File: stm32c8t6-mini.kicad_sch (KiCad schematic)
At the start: 40 parts, among them J1 Conn_01x07_Pin, J2 Conn_01x18_Pin, J3 Conn_01x18_Pin, P1 USB, SW1 Reset, SW2 BOOT0, U1 STM32F103C8Tx, U2 AMS1117, U3 USBLC6-2SC6, Y1 8MHz, Y2 32.768kHz

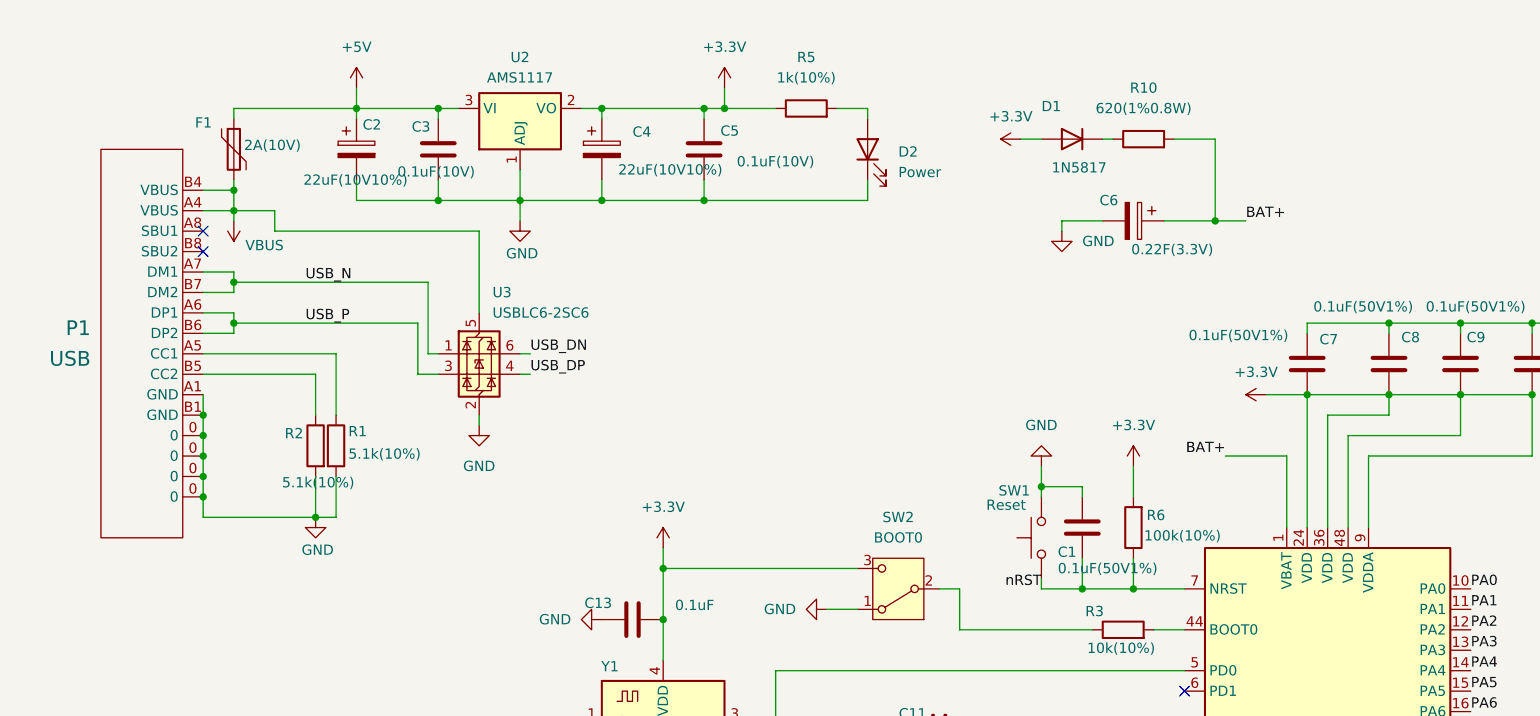
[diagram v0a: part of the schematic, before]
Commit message: Replace the USB-C socket type
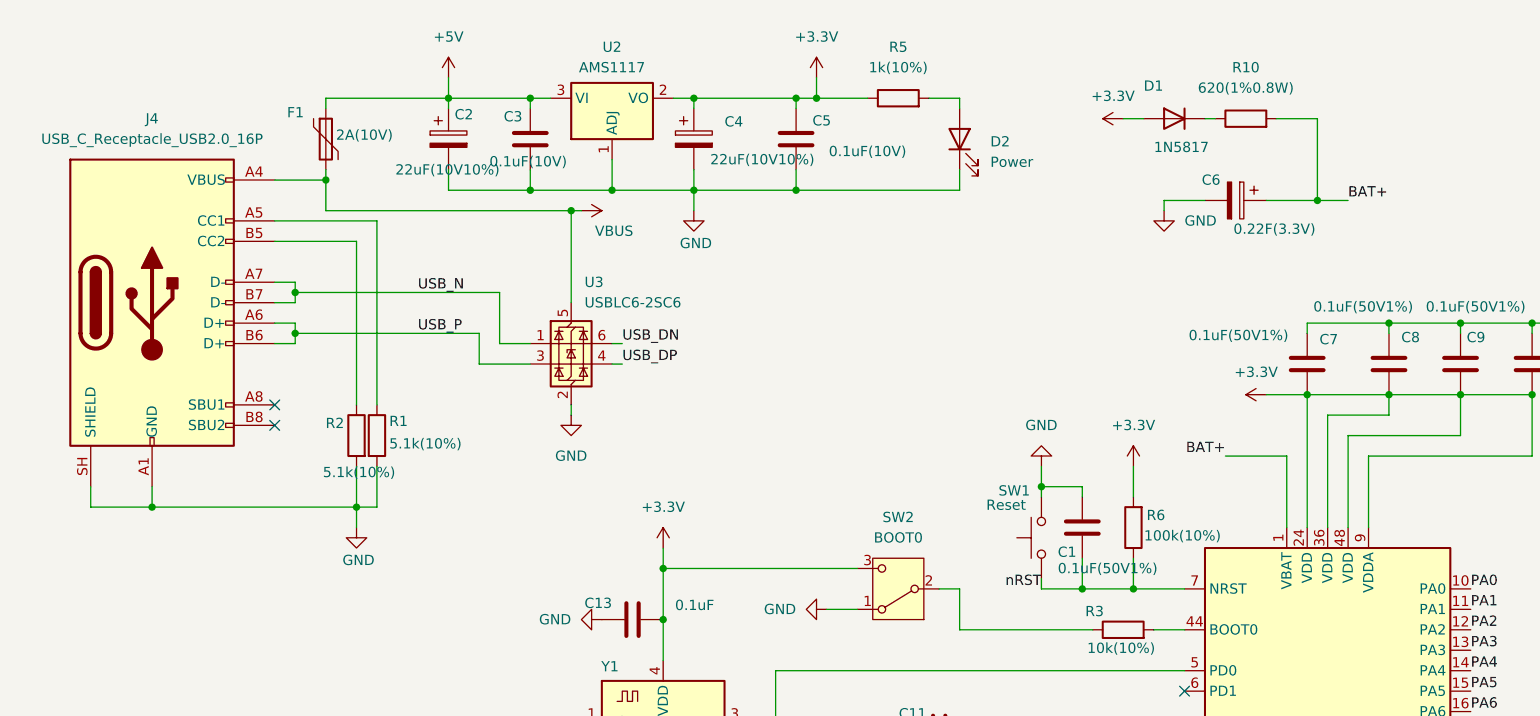
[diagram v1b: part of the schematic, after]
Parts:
- removed P1: USB, WCH:TYPE-C-Receptacle-2.0, symbol WCH:USBC-REC
- added J4: USB_C_Receptacle_USB2.0_16P, Connector_USB:USB_C_Receptacle_HRO_TYPE-C-31-M-12, symbol Connector:USB_C_Receptacle_USB2.0_16P
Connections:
- net GND: now also J4.A1 (GND), J4.A12 (GND), J4.B1 (GND), J4.B12 (GND), J4.SH (SHIELD)
- net USB_N: now also J4.A7 (D-), J4.B7 (D-)
- net USB_P: now also J4.A6 (D+), J4.B6 (D+)
- net VBUS: now also J4.A4 (VBUS), J4.A9 (VBUS), J4.B4 (VBUS), J4.B9 (VBUS)
- net at R1.1: now also J4.A5 (CC1)
- net at R2.1: now also J4.B5 (CC2)
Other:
- moved on the sheet: C2, C3, C4, C5, C6, D1, D2, F1, R1, R10, R2, R5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

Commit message: Add description to the sheet
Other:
- company: (none) -> Yongci
- title: (none) -> STM32C8T6-Mini
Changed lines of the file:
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@@
 	(generator_version "10.0")
 	(paper "A4")
+	(title_block
+		(title "STM32C8T6-Mini")
+		(date "2026-09-13")
+		(rev "v1.2")
+		(company "Yongci")
+		(comment 1 "zhuyongci@github.com")
+	)
 	(junction
 		(at 45.72 52.07)

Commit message: Replace some components: 1. Replace the RTC super-capacitance to a 5.5mAh battery. 2. Replace the 1N5817-diode to 1SS367. 3. Replace the resister size from 0805 to 0603(0.1w~).
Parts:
- removed C6: 0.22F(3.3V), Battery:BatteryHolder_Seiko_MS621F, symbol Device:C_Polarized
- added BT1: MS621FE,5.5mAh,3.3V, Battery:BatteryHolder_Seiko_MS621F, symbol Device:Battery_Cell
- D1: value 1N5817 -> 1SS367; footprint Diode_SMD:D_SOD-123 -> Diode_SMD:D_SOD-323
- R10: value 620(1%0.8W) -> 620R(1%0.1W); footprint Resistor_SMD:R_0805_2012Metric -> Resistor_SMD:R_0603_1608Metric
- renumbered C11 to C10, C12 to C11, C13 to C12, C7 to C6, C8 to C7, C9 to C8, C10 to C9
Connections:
- net BAT+: now also BT1.1 (+)
- net GND: now also BT1.2 (-)
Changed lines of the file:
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@@
 	(title_block
 		(title "STM32C8T6-Mini")
-		(date "2026-09-13")
-		(rev "v1.2")
+		(date "2026-09-20")
+		(rev "v1.3")
 		(company "Yongci")
 		(comment 1 "zhuyongci@hotmail.com")
@@
 		(in_pos_files yes)
 		(dnp no)
-		(property "Reference" "C13"
+		(property "Reference" "C12"
 			(at 85.09 85.598 90)
 			(show_name no)
@@
 			(project "stm32c8t6-mini"
 				(path "/dd0baac2-12ea-4b58-abcb-703e6e71325e"
-					(reference "C13")
+					(reference "C12")
 					(unit 1)
 				)
@@
 			)
 		)
-		(property "Value" "1N5817"
+		(property "Value" "1SS367"
 			(at 152.4 28.956 0)
 			(show_name no)
@@
 			)
 		)
-		(property "Footprint" "Diode_SMD:D_SOD-123"
+		(property "Footprint" "Diode_SMD:D_SOD-323"
 			(at 154.94 29.845 0)
 			(hide yes)
@@
 			)
 		)
-		(property "Datasheet" "https://www.vishay.com/docs/85748/1n4148w.pdf"
+		(property "Datasheet" "https://www.alldatasheet.com/html-pdf/29822/TOSHIBA/1SS367/495/2/1SS367.html"
 			(at 154.94 25.4 0)
 			(hide yes)
@@
 			)
 		)
-		(property "Description" "75V 0.15A Fast Switching Diode, SOD-123"
+		(property "Description" "10V 100mA Fast Diode, SOD-323"
 			(at 154.94 25.4 0)
 			(hide yes)
@@
 		(in_pos_files yes)
 		(dnp no)
-		(property "Reference" "C11"
+		(property "Reference" "C10"
 			(at 122.428 99.314 90)
 			(show_name no)
@@
 			(project "stm32c8t6-mini"
 				(path "/dd0baac2-12ea-4b58-abcb-703e6e71325e"
-					(reference "C11")
+					(reference "C10")
 					(unit 1)
 				)
@@
 			)
 		)
-		(property "Value" "620(1%0.8W)"
+		(property "Value" "620R(1%0.1W)"
 			(at 163.83 21.59 90)
 			(show_name no)
@@
 			)
 		)
-		(property "Footprint" "Resistor_SMD:R_0805_2012Metric"
+		(property "Footprint" "Resistor_SMD:R_0603_1608Metric"
 			(at 163.83 27.178 90)
 			(hide yes)
@@
 		(in_pos_files yes)
 		(dnp no)
-		(property "Reference" "C10"
+		(property "Reference" "C9"
 			(at 200.66 52.578 0)
 			(show_name no)
@@
 			(project "stm32c8t6-mini"
 				(path "/dd0baac2-12ea-4b58-abcb-703e6e71325e"
-					(reference "C10")
-					(unit 1)
-				)
-			)
-		)
-	)
-	(symbol
-		(lib_id "Device:C_Polarized")
-		(at 162.56 35.56 270)
-		(unit 1)
-		(body_style 1)
-		(exclude_from_sim no)
-		(in_bom yes)
-		(on_board yes)
-		(in_pos_files yes)
-		(dnp no)
-		(property "Reference" "C6"
-			(at 159.512 33.02 90)
-			(show_name no)
-			(do_not_autoplace no)
-			(effects
-				(font
-					(size 1.27 1.27)
-				)
-			)
-		)
-		(property "Value" "0.22F(3.3V)"
-			(at 167.386 39.116 90)
-			(show_name no)
-			(do_not_autoplace no)
-			(effects
-				(font
-					(size 1.27 1.27)
-				)
-			)
-		)
-		(property "Footprint" "Battery:BatteryHolder_Seiko_MS621F"
-			(at 158.75 36.5252 0)
-			(hide yes)
-			(show_name no)
-			(do_not_autoplace no)
-			(effects
-				(font
-					(size 1.27 1.27)
-				)
-			)
-		)
-		(property "Datasheet" ""
-			(at 162.56 35.56 0)
-			(hide yes)
-			(show_name no)
-			(do_not_autoplace no)
-			(effects
-				(font
-					(size 1.27 1.27)
-				)
-			)
-		)
-		(property "Description" "Polarized capacitor"
-			(at 162.56 35.56 0)
-			(hide yes)
-			(show_name no)
-			(do_not_autoplace no)
-			(effects
-				(font
-					(size 1.27 1.27)
-				)
-			)
-		)
-		(pin "2"
-		)
-		(pin "1"
-		)
-		(instances
-			(project "stm32c8t6-mini"
-				(path "/dd0baac2-12ea-4b58-abcb-703e6e71325e"
-					(reference "C6")
+					(reference "C9")
 					(unit 1)
 				)
@@
 		(in_pos_files yes)
 		(dnp no)
-		(property "Reference" "C8"
+		(property "Reference" "C7"
 			(at 183.134 52.578 0)
 			(show_name no)
@@
 			(project "stm32c8t6-mini"
 				(path "/dd0baac2-12ea-4b58-abcb-703e6e71325e"
-					(reference "C8")
+					(reference "C7")
 					(unit 1)
 				)
@@
 	)
 	(symbol
+		(lib_id "Device:Battery_Cell")
+		(at 161.29 35.56 270)
+		(unit 1)
+		(body_style 1)
+		(exclude_from_sim no)
+		(in_bom yes)
+		(on_board yes)
+		(in_pos_files yes)
+		(dnp no)
+		(property "Reference" "BT1"
+			(at 162.814 31.496 90)
+			(show_name no)
+			(do_not_autoplace no)
+			(effects
+				(font
+					(size 1.27 1.27)
+				)
+			)
+		)
+		(property "Value" "MS621FE,5.5mAh,3.3V"
+			(at 171.958 39.37 90)
+			(show_name no)
+			(do_not_autoplace no)
+			(effects
+				(font
+					(size 1.27 1.27)
+				)
+			)
+		)
+		(property "Footprint" "Battery:BatteryHolder_Seiko_MS621F"
+			(at 162.814 35.56 90)
+			(hide yes)
+			(show_name no)
+			(do_not_autoplace no)
+			(effects
+				(font
+					(size 1.27 1.27)
+				)
+			)
+		)
+		(property "Datasheet" ""
+			(at 162.814 35.56 90)
+			(hide yes)
+			(show_name no)
+			(do_not_autoplace no)
+			(effects
+				(font
+					(size 1.27 1.27)
+				)
+			)
+		)
+		(property "Description" "Single-cell battery"
+			(at 161.29 35.56 0)
+			(hide yes)
+			(show_name no)
+			(do_not_autoplace no)
+			(effects
+				(font
+					(size 1.27 1.27)
+				)
+			)
+		)
+		(property "Sim.Device" "V"
+			(at 161.29 35.56 0)
+			(hide yes)
+			(show_name no)
+			(do_not_autoplace no)
+			(effects
+				(font
+					(size 1.27 1.27)
+				)
+			)
+		)
+		(property "Sim.Type" "DC"
+			(at 161.29 35.56 0)
+			(hide yes)
+			(show_name no)
+			(do_not_autoplace no)
+			(effects
+				(font
+					(size 1.27 1.27)
+				)
+			)
+		)
+		(property "Sim.Pins" "1=+ 2=-"
+			(at 161.29 35.56 0)
+			(hide yes)
+			(show_name no)
+			(do_not_autoplace no)
+			(effects
+				(font
+					(size 1.27 1.27)
+				)
+			)
+		)
+		(pin "2"
+		)
+		(pin "1"
+		)
+		(instances
+			(project "stm32c8t6-mini"
+				(path "/dd0baac2-12ea-4b58-abcb-703e6e71325e"
+					(reference "BT1")
+					(unit 1)
+				)
+			)
+		)
+	)
+	(symbol
 		(lib_id "Connector:USB_C_Receptacle_USB2.0_16P")
 		(at 27.94 48.26 0)
@@
 		(in_pos_files yes)
 		(dnp no)
-		(property "Reference" "C7"
+		(property "Reference" "C6"
 			(at 172.974 52.832 0)
 			(show_name no)
@@
 			(project "stm32c8t6-mini"
 				(path "/dd0baac2-12ea-4b58-abcb-703e6e71325e"
-					(reference "C7")
+					(reference "C6")
 					(unit 1)
 				)
@@
 		(in_pos_files yes)
 		(dnp no)
-		(property "Reference" "C9"
+		(property "Reference" "C8"
 			(at 191.262 52.578 0)
 			(show_name no)
@@
 			(project "stm32c8t6-mini"
 				(path "/dd0baac2-12ea-4b58-abcb-703e6e71325e"
-					(reference "C9")
+					(reference "C8")
 					(unit 1)
 				)
@@
 		(in_pos_files yes)
 		(dnp no)
-		(property "Reference" "C12"
+		(property "Reference" "C11"
 			(at 122.174 107.696 90)
 			(show_name no)
@@
 			(project "stm32c8t6-mini"
 				(path "/dd0baac2-12ea-4b58-abcb-703e6e71325e"
-					(reference "C12")
+					(reference "C11")
 					(unit 1)
 				)
